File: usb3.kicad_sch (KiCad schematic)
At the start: 41 parts, among them J5 WE_632723300011_alt_symbol, Q4 NX138BKMYL, U17 HD3SS3220, U18 AP22615, U19 TPD4E05U06QDQARQ1, U20 TPD4E05U06QDQARQ1, U21 TPD4E05U06QDQARQ1

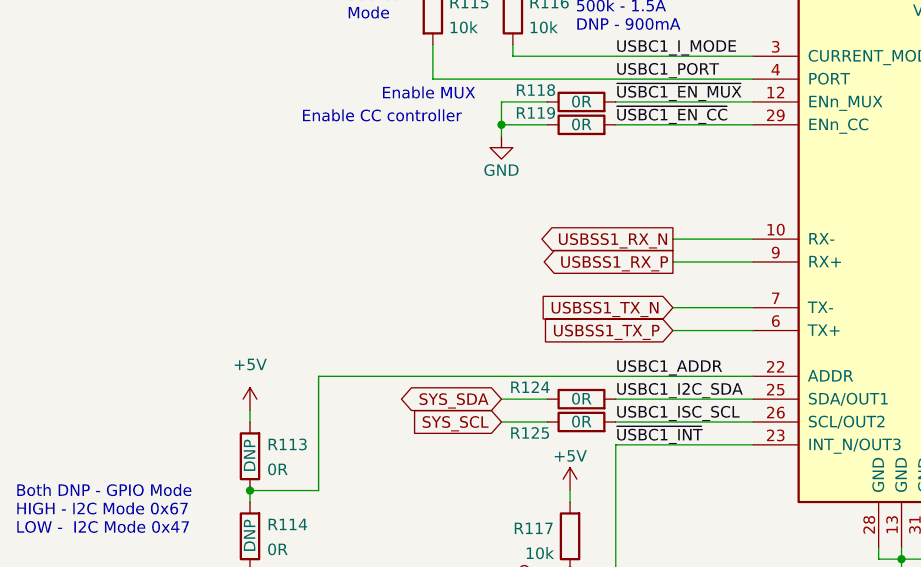
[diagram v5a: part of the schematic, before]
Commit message: Routed USB SS for USB-C connectors
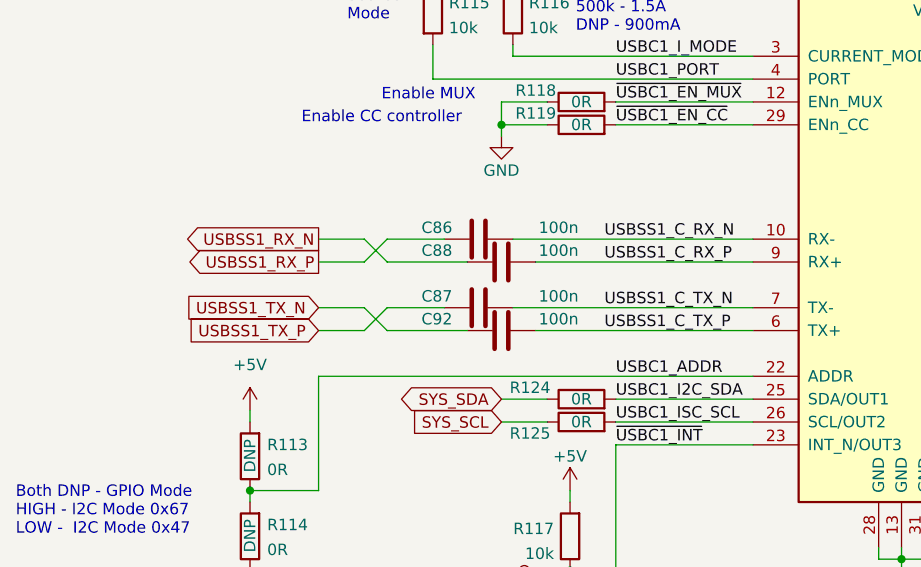
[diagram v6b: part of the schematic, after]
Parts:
- added C86, C87, C88, C92: C_100n_0402, antmicro-footprints:0402-cap, symbol antmicroCapacitors0402:C_100n_0402
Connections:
- net USBSS1_RX_N: now also C88.1; no longer U17.10 (RX-)
- net USBSS1_RX_P: now also C86.1; no longer U17.9 (RX+)
- net USBSS1_TX_N: now also C92.1; no longer U17.7 (TX-)
- net USBSS1_TX_P: now also C87.1; no longer U17.6 (TX+)
- new net USBSS1_C_RX_N: C86.2, U17.10 (RX-)
- new net USBSS1_C_RX_P: C88.2, U17.9 (RX+)
- new net USBSS1_C_TX_N: C87.2, U17.7 (TX-)
- new net USBSS1_C_TX_P: C92.2, U17.6 (TX+)

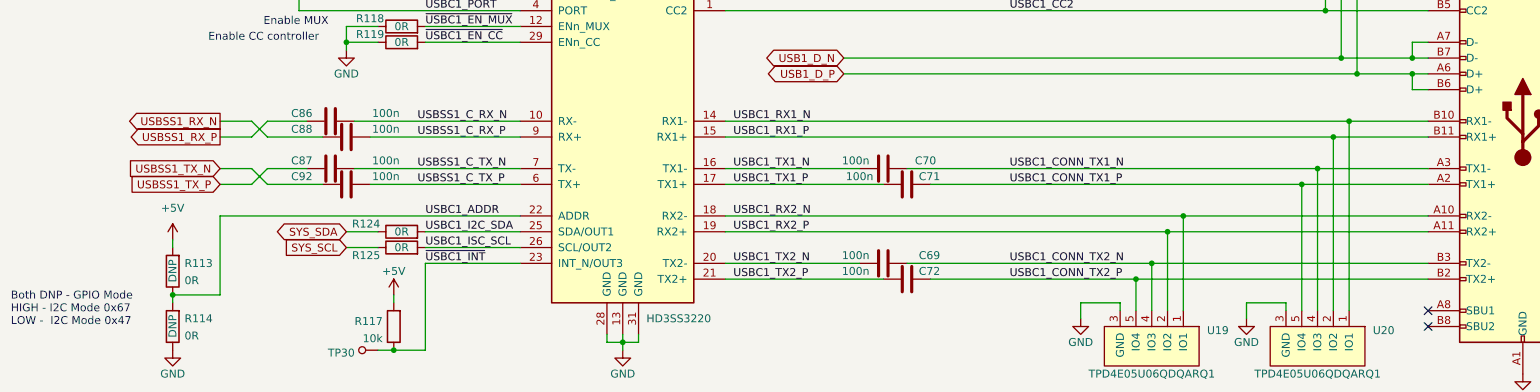
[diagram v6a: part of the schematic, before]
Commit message: rerouted USB SS
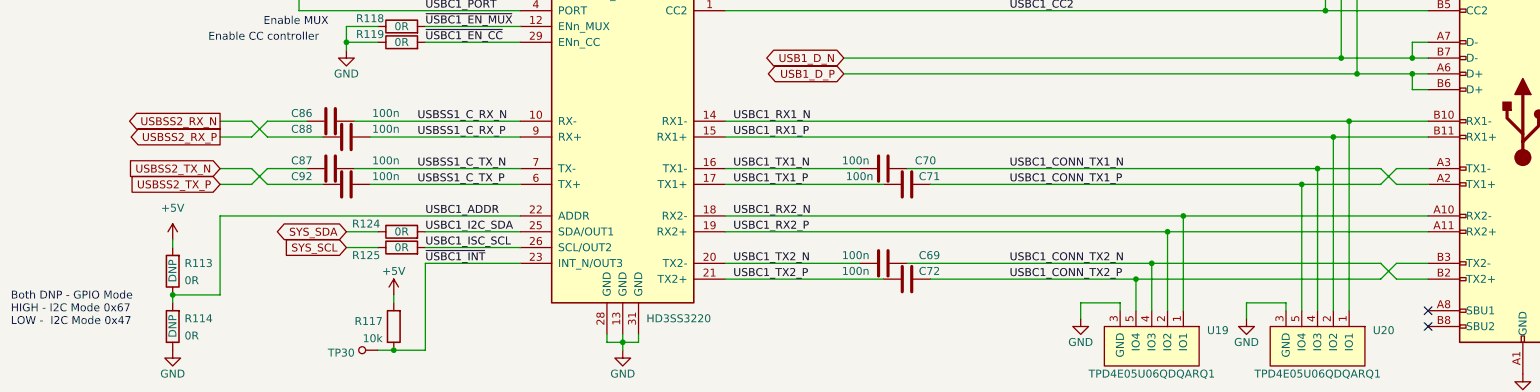
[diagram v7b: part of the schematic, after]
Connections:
- net USBC1_CONN_TX1_N: now also J5.A2 (TX1+); no longer J5.A3 (TX1-)
- net USBC1_CONN_TX1_P: now also J5.A3 (TX1-); no longer J5.A2 (TX1+)
- net USBC1_CONN_TX2_N: now also J5.B2 (TX2+); no longer J5.B3 (TX2-)
- net USBC1_CONN_TX2_P: now also J5.B3 (TX2-); no longer J5.B2 (TX2+)
- net USBSS1_RX_N renamed USBSS2_RX_N
- net USBSS1_RX_P renamed USBSS2_RX_P
- net USBSS1_TX_N renamed USBSS2_TX_N
- net USBSS1_TX_P renamed USBSS2_TX_P
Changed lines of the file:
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@@
     (stroke (width 0) (type default) (color 0 0 0 0))
   )
-  (wire (pts (xy 271.78 162.56) (xy 289.56 162.56))
+  (wire (pts (xy 271.78 162.56) (xy 281.94 162.56))
     (stroke (width 0) (type default) (color 0 0 0 0))
   )
@@
     (stroke (width 0) (type default) (color 0 0 0 0))
   )
+  (wire (pts (xy 281.94 162.56) (xy 284.48 165.1))
+    (stroke (width 0) (type default) (color 0 0 0 0))
+  )
   (wire (pts (xy 209.55 165.1) (xy 269.24 165.1))
     (stroke (width 0) (type default) (color 0 0 0 0))
@@
     (stroke (width 0) (type default) (color 0 0 0 0))
   )
+  (wire (pts (xy 284.48 162.56) (xy 289.56 162.56))
+    (stroke (width 0) (type default) (color 0 0 0 0))
+  )
   (wire (pts (xy 172.72 96.52) (xy 172.72 97.79))
     (stroke (width 0) (type default) (color 0 0 0 0))
@@
     (stroke (width 0) (type default) (color 0 0 0 0))
   )
+  (wire (pts (xy 284.48 165.1) (xy 289.56 165.1))
+    (stroke (width 0) (type default) (color 0 0 0 0))
+  )
   (wire (pts (xy 128.27 142.24) (xy 143.51 142.24))
     (stroke (width 0) (type default) (color 0 0 0 0))
@@
     (stroke (width 0) (type default) (color 0 0 0 0))
   )
-  (wire (pts (xy 269.24 165.1) (xy 289.56 165.1))
+  (wire (pts (xy 269.24 165.1) (xy 281.94 165.1))
     (stroke (width 0) (type default) (color 0 0 0 0))
   )
@@
     (stroke (width 0) (type default) (color 0 0 0 0))
   )
+  (wire (pts (xy 284.48 180.34) (xy 289.56 180.34))
+    (stroke (width 0) (type default) (color 0 0 0 0))
+  )
   (wire (pts (xy 119.38 157.48) (xy 143.51 157.48))
     (stroke (width 0) (type default) (color 0 0 0 0))
@@
     (stroke (width 0) (type default) (color 0 0 0 0))
   )
+  (wire (pts (xy 284.48 177.8) (xy 281.94 180.34))
+    (stroke (width 0) (type default) (color 0 0 0 0))
+  )
   (wire (pts (xy 199.39 118.11) (xy 199.39 121.92))
     (stroke (width 0) (type default) (color 0 0 0 0))
@@
     (stroke (width 0) (type default) (color 0 0 0 0))
   )
-  (wire (pts (xy 245.11 177.8) (xy 289.56 177.8))
+  (wire (pts (xy 245.11 177.8) (xy 281.94 177.8))
     (stroke (width 0) (type default) (color 0 0 0 0))
   )
@@
     (stroke (width 0) (type default) (color 0 0 0 0))
   )
+  (wire (pts (xy 284.48 162.56) (xy 281.94 165.1))
+    (stroke (width 0) (type default) (color 0 0 0 0))
+  )
   (wire (pts (xy 260.35 184.15) (xy 266.7 184.15))
     (stroke (width 0) (type default) (color 0 0 0 0))
@@
     (stroke (width 0) (type default) (color 0 0 0 0))
   )
+  (wire (pts (xy 281.94 177.8) (xy 284.48 180.34))
+    (stroke (width 0) (type default) (color 0 0 0 0))
+  )
   (wire (pts (xy 128.27 177.8) (xy 143.51 177.8))
     (stroke (width 0) (type default) (color 0 0 0 0))
@@
     (stroke (width 0) (type default) (color 0 0 0 0))
   )
-  (wire (pts (xy 242.57 180.34) (xy 289.56 180.34))
+  (wire (pts (xy 242.57 180.34) (xy 281.94 180.34))
+    (stroke (width 0) (type default) (color 0 0 0 0))
+  )
+  (wire (pts (xy 284.48 177.8) (xy 289.56 177.8))
     (stroke (width 0) (type default) (color 0 0 0 0))
   )
@@
     )
   )
-  (global_label "USBSS1_RX_P" (shape output) (at 95.25 157.48 180)
-    (effects (font (size 1.27 1.27)) (justify right))
-    (property "Intersheet References" "${INTERSHEET_REFS}" (id 0) (at 78.74 157.48 0)
-      (effects (font (size 1.1 1.1)) (justify right))
-    )
-  )
   (global_label "USBC1_PEN" (shape input) (at 214.63 100.33 180)
     (effects (font (size 1.27 1.27)) (justify right))
@@
     )
   )
-  (global_label "USBSS1_RX_N" (shape output) (at 95.25 154.94 180)
+  (global_label "USBSS2_TX_P" (shape input) (at 95.25 165.1 180)
     (effects (font (size 1.27 1.27)) (justify right))
-    (property "Intersheet References" "${INTERSHEET_REFS}" (id 0) (at 78.74 154.94 0)
-      (effects (font (size 1.1 1.1)) (justify right))
+    (property "Intersheet References" "${INTERSHEET_REFS}" (id 0) (at 76.835 165.1 0)
+      (effects (font (size 1.27 1.27)) (justify right))
     )
   )
-  (global_label "USBSS1_TX_P" (shape input) (at 95.25 165.1 180)
+  (global_label "USBSS2_TX_N" (shape input) (at 95.25 162.56 180)
     (effects (font (size 1.27 1.27)) (justify right))
-    (property "Intersheet References" "${INTERSHEET_REFS}" (id 0) (at 78.74 165.1 0)
-      (effects (font (size 1.1 1.1)) (justify right))
+    (property "Intersheet References" "${INTERSHEET_REFS}" (id 0) (at 76.835 162.56 0)
+      (effects (font (size 1.27 1.27)) (justify right))
     )
   )
-  (global_label "USBSS1_TX_N" (shape input) (at 95.25 162.56 180)
+  (global_label "USBSS2_RX_P" (shape output) (at 95.25 157.48 180)
     (effects (font (size 1.27 1.27)) (justify right))
-    (property "Intersheet References" "${INTERSHEET_REFS}" (id 0) (at 78.74 162.56 0)
+    (property "Intersheet References" "${INTERSHEET_REFS}" (id 0) (at 76.2 157.48 0)
       (effects (font (size 1.1 1.1)) (justify right))
     )
@@
       (effects (font (size 1.1 1.1)) (justify right))
     )
+  )
+  (global_label "USBSS2_RX_N" (shape output) (at 95.25 154.94 180)
+    (effects (font (size 1.27 1.27)) (justify right))
+    (property "Intersheet References" "${INTERSHEET_REFS}" (id 0) (at 76.2 154.94 0)
+      (effects (font (size 1.1 1.1)) (justify right))
+    )

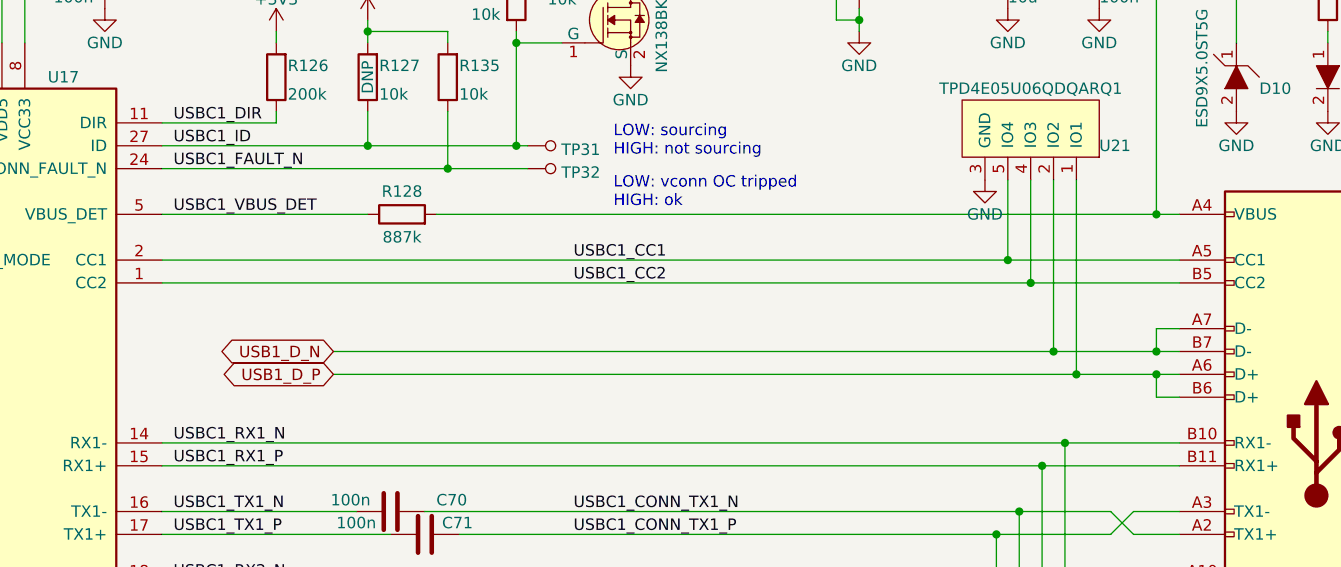
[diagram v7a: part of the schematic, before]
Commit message: Routed USB connector
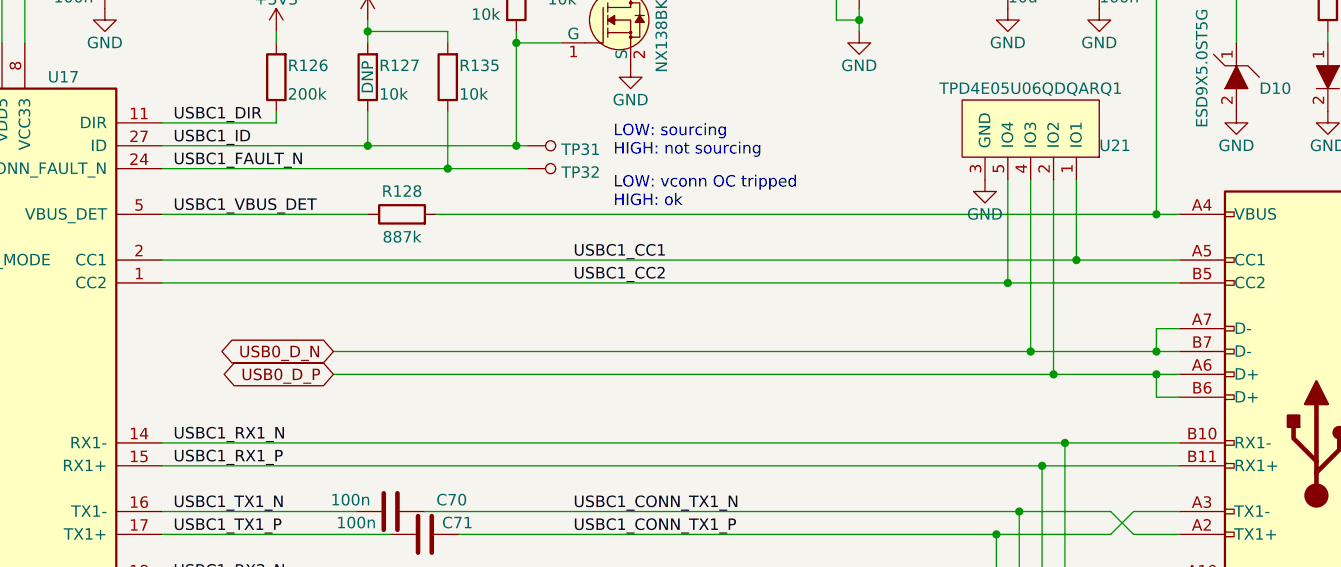
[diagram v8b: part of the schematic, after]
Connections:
- net USBC1_CC1: now also U21.1 (IO1), U21.10 (IO1); no longer U21.5 (IO4), U21.6 (IO4)
- net USBC1_CC2: now also U21.5 (IO4), U21.6 (IO4); no longer U21.4 (IO3), U21.7 (IO3)
- net USB1_D_N renamed USB0_D_N
- net USB0_D_N: now also U21.4 (IO3), U21.7 (IO3); no longer U21.2 (IO2), U21.9 (IO2)
- net USB1_D_P renamed USB0_D_P
- net USB0_D_P: now also U21.2 (IO2), U21.9 (IO2); no longer U21.1 (IO1), U21.10 (IO1)
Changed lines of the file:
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@@
   (junction (at 87.63 182.88) (diameter 0) (color 0 0 0 0)
   )
-  (junction (at 278.13 147.32) (diameter 0) (color 0 0 0 0)
-  )
   (junction (at 123.19 191.77) (diameter 0) (color 0 0 0 0)
   )
-  (junction (at 275.59 144.78) (diameter 0) (color 0 0 0 0)
-  )
   (junction (at 287.02 95.25) (diameter 0) (color 0 0 0 0)
   )
+  (junction (at 270.51 137.16) (diameter 0) (color 0 0 0 0)
+  )
   (junction (at 140.97 97.79) (diameter 0) (color 0 0 0 0)
   )
@@
   (junction (at 274.32 157.48) (diameter 0) (color 0 0 0 0)
   )
+  (junction (at 273.05 144.78) (diameter 0) (color 0 0 0 0)
+  )
   (junction (at 287.02 144.78) (diameter 0) (color 0 0 0 0)
   )
   (junction (at 287.02 147.32) (diameter 0) (color 0 0 0 0)
   )
+  (junction (at 275.59 147.32) (diameter 0) (color 0 0 0 0)
+  )
   (junction (at 199.39 109.22) (diameter 0) (color 0 0 0 0)
   )
-  (junction (at 273.05 137.16) (diameter 0) (color 0 0 0 0)
-  )
   (junction (at 250.19 170.18) (diameter 0) (color 0 0 0 0)
   )
@@
   (junction (at 295.91 95.25) (diameter 0) (color 0 0 0 0)
   )
-  (junction (at 270.51 134.62) (diameter 0) (color 0 0 0 0)
-  )
   (junction (at 254 107.95) (diameter 0) (color 0 0 0 0)
+  )
+  (junction (at 278.13 134.62) (diameter 0) (color 0 0 0 0)
   )
   (junction (at 280.67 95.25) (diameter 0) (color 0 0 0 0)
@@
     (stroke (width 0) (type default) (color 0 0 0 0))
   )
+  (wire (pts (xy 278.13 125.73) (xy 278.13 134.62))
+    (stroke (width 0) (type default) (color 0 0 0 0))
+  )
   (wire (pts (xy 199.39 109.22) (xy 208.28 109.22))
     (stroke (width 0) (type default) (color 0 0 0 0))
@@
     (stroke (width 0) (type default) (color 0 0 0 0))
   )
+  (wire (pts (xy 273.05 125.73) (xy 273.05 144.78))
+    (stroke (width 0) (type default) (color 0 0 0 0))
+  )
   (wire (pts (xy 172.72 97.79) (xy 170.18 97.79))
     (stroke (width 0) (type default) (color 0 0 0 0))
@@
     (stroke (width 0) (type default) (color 0 0 0 0))
   )
-  (wire (pts (xy 273.05 137.16) (xy 289.56 137.16))
-    (stroke (width 0) (type default) (color 0 0 0 0))
-  )
   (wire (pts (xy 287.02 129.54) (xy 289.56 129.54))
     (stroke (width 0) (type default) (color 0 0 0 0))
@@
     (stroke (width 0) (type default) (color 0 0 0 0))
   )
-  (wire (pts (xy 273.05 125.73) (xy 273.05 137.16))
-    (stroke (width 0) (type default) (color 0 0 0 0))
-  )
   (wire (pts (xy 176.53 121.92) (xy 199.39 121.92))
     (stroke (width 0) (type default) (color 0 0 0 0))
@@
     (stroke (width 0) (type default) (color 0 0 0 0))
   )
-  (wire (pts (xy 195.58 144.78) (xy 275.59 144.78))
+  (wire (pts (xy 195.58 144.78) (xy 273.05 144.78))
     (stroke (width 0) (type default) (color 0 0 0 0))
   )
@@
     (stroke (width 0) (type default) (color 0 0 0 0))
   )
-  (wire (pts (xy 275.59 144.78) (xy 287.02 144.78))
-    (stroke (width 0) (type default) (color 0 0 0 0))
-  )
   (wire (pts (xy 270.51 95.25) (xy 270.51 99.06))
     (stroke (width 0) (type default) (color 0 0 0 0))
@@
     (stroke (width 0) (type default) (color 0 0 0 0))
   )
-  (wire (pts (xy 278.13 147.32) (xy 287.02 147.32))
+  (wire (pts (xy 195.58 147.32) (xy 275.59 147.32))
     (stroke (width 0) (type default) (color 0 0 0 0))
   )
@@
     (stroke (width 0) (type default) (color 0 0 0 0))
   )
-  (wire (pts (xy 176.53 134.62) (xy 270.51 134.62))
-    (stroke (width 0) (type default) (color 0 0 0 0))
-  )
   (wire (pts (xy 157.48 190.5) (xy 160.02 190.5))
     (stroke (width 0) (type default) (color 0 0 0 0))
@@
     (stroke (width 0) (type default) (color 0 0 0 0))
   )
+  (wire (pts (xy 273.05 144.78) (xy 287.02 144.78))
+    (stroke (width 0) (type default) (color 0 0 0 0))
+  )
   (wire (pts (xy 87.63 182.88) (xy 87.63 184.15))
     (stroke (width 0) (type default) (color 0 0 0 0))
@@
     (stroke (width 0) (type default) (color 0 0 0 0))
   )
+  (wire (pts (xy 270.51 125.73) (xy 270.51 137.16))
+    (stroke (width 0) (type default) (color 0 0 0 0))
+  )
   (wire (pts (xy 189.23 109.22) (xy 189.23 110.49))
     (stroke (width 0) (type default) (color 0 0 0 0))
@@
     (stroke (width 0) (type default) (color 0 0 0 0))
   )
-  (wire (pts (xy 176.53 137.16) (xy 273.05 137.16))
-    (stroke (width 0) (type default) (color 0 0 0 0))
-  )
   (wire (pts (xy 199.39 129.54) (xy 176.53 129.54))
     (stroke (width 0) (type default) (color 0 0 0 0))
@@
     (stroke (width 0) (type default) (color 0 0 0 0))
   )
-  (wire (pts (xy 195.58 147.32) (xy 278.13 147.32))
-    (stroke (width 0) (type default) (color 0 0 0 0))
-  )
-  (wire (pts (xy 270.51 125.73) (xy 270.51 134.62))
+  (wire (pts (xy 176.53 137.16) (xy 270.51 137.16))
     (stroke (width 0) (type default) (color 0 0 0 0))
   )
@@
     (stroke (width 0) (type default) (color 0 0 0 0))
   )
+  (wire (pts (xy 176.53 134.62) (xy 278.13 134.62))
+    (stroke (width 0) (type default) (color 0 0 0 0))
+  )
   (wire (pts (xy 128.27 177.8) (xy 143.51 177.8))
     (stroke (width 0) (type default) (color 0 0 0 0))
@@
     (stroke (width 0) (type default) (color 0 0 0 0))
   )
-  (wire (pts (xy 278.13 125.73) (xy 278.13 147.32))
-    (stroke (width 0) (type default) (color 0 0 0 0))
-  )
   (wire (pts (xy 295.91 95.25) (xy 295.91 110.49))
     (stroke (width 0) (type default) (color 0 0 0 0))
@@
     (stroke (width 0) (type default) (color 0 0 0 0))
   )
+  (wire (pts (xy 275.59 125.73) (xy 275.59 147.32))
+    (stroke (width 0) (type default) (color 0 0 0 0))
+  )
   (wire (pts (xy 157.48 189.23) (xy 157.48 190.5))
     (stroke (width 0) (type default) (color 0 0 0 0))
   )
-  (wire (pts (xy 270.51 134.62) (xy 289.56 134.62))
-    (stroke (width 0) (type default) (color 0 0 0 0))
-  )
   (wire (pts (xy 100.33 154.94) (xy 95.25 154.94))
     (stroke (width 0) (type default) (color 0 0 0 0))
@@
     (stroke (width 0) (type default) (color 0 0 0 0))
   )
+  (wire (pts (xy 275.59 147.32) (xy 287.02 147.32))
+    (stroke (width 0) (type default) (color 0 0 0 0))
+  )
   (wire (pts (xy 276.86 154.94) (xy 276.86 185.42))
     (stroke (width 0) (type default) (color 0 0 0 0))
@@
     (stroke (width 0) (type default) (color 0 0 0 0))
   )
+  (wire (pts (xy 270.51 137.16) (xy 289.56 137.16))
+    (stroke (width 0) (type default) (color 0 0 0 0))
+  )
   (wire (pts (xy 228.6 86.36) (xy 231.14 86.36))
     (stroke (width 0) (type default) (color 0 0 0 0))
@@
     (stroke (width 0) (type default) (color 0 0 0 0))
   )
-  (wire (pts (xy 275.59 125.73) (xy 275.59 144.78))
-    (stroke (width 0) (type default) (color 0 0 0 0))
-  )
   (wire (pts (xy 176.53 177.8) (xy 198.12 177.8))
     (stroke (width 0) (type default) (color 0 0 0 0))
@@
   )
   (wire (pts (xy 120.65 191.77) (xy 123.19 191.77))
+    (stroke (width 0) (type default) (color 0 0 0 0))
+  )
+  (wire (pts (xy 278.13 134.62) (xy 289.56 134.62))
     (stroke (width 0) (type default) (color 0 0 0 0))
   )
@@
     (effects (font (size 1.27 1.27)) (justify left bottom))
   )
-  (global_label "USB1_D_P" (shape bidirectional) (at 195.58 147.32 180)
-    (effects (font (size 1.27 1.27)) (justify right))
-    (property "Intersheet References" "${INTERSHEET_REFS}" (id 0) (at 181.61 147.32 0)
-      (effects (font (size 1.1 1.1)) (justify right))
-    )
-  )
   (global_label "SYS_SCL" (shape input) (at 115.57 175.26 180)
     (effects (font (size 1.27 1.27)) (justify right))
@@
     )
   )
+  (global_label "USB0_D_P" (shape bidirectional) (at 195.58 147.32 180)
+    (effects (font (size 1.27 1.27)) (justify right))
+    (property "Intersheet References" "${INTERSHEET_REFS}" (id 0) (at 182.245 147.32 0)
+      (effects (font (size 1.1 1.1)) (justify right))
+    )
+  )
+  (global_label "USB0_D_N" (shape bidirectional) (at 195.58 144.78 180)
+    (effects (font (size 1.27 1.27)) (justify right))
+    (property "Intersheet References" "${INTERSHEET_REFS}" (id 0) (at 182.245 144.78 0)
+      (effects (font (size 1.1 1.1)) (justify right))
+    )
+  )
   (global_label "USBSS2_RX_P" (shape output) (at 95.25 157.48 180)
     (effects (font (size 1.27 1.27)) (justify right))
@@
       (effects (font (size 1.1 1.1)) (justify right))
     )
-  )
-  (global_label "USB1_D_N" (shape bidirectional) (at 195.58 144.78 180)
-    (effects (font (size 1.27 1.27)) (justify right))
-    (property "Intersheet References" "${INTERSHEET_REFS}" (id 0) (at 181.5576 144.78 0)
-      (effects (font (size 1.1 1.1)) (justify right))
-    )
